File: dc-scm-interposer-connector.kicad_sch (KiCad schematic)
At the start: 19 parts, among them J2001 PinHeader_2x6_P2.54mm_Drill1.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

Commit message: [#103910] Update power section
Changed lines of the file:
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@@
-	(wire
-		(pts
-			(xy 142.24 85.09) (xy 142.24 86.36)
-		)
-		(stroke
-			(width 0)
-			(type default)
-		)
-	)
 	(wire
 		(pts
@@
 	(wire
 		(pts
-			(xy 142.24 88.9) (xy 144.78 88.9)
-		)
-		(stroke
-			(width 0)
-			(type default)
-		)
-	)
-	(wire
-		(pts
 			(xy 149.86 115.57) (xy 152.4 115.57)
 		)
@@
 	(wire
 		(pts
-			(xy 140.97 85.09) (xy 142.24 85.09)
+			(xy 127 86.36) (xy 144.78 86.36)
 		)
 		(stroke
@@
 		)
 	)
-	(wire
-		(pts
-			(xy 142.24 86.36) (xy 144.78 86.36)
-		)
-		(stroke
-			(width 0)
-			(type default)
-		)
-	)
 	(bus
 		(pts
@@
 	(wire
 		(pts
-			(xy 142.24 87.63) (xy 142.24 88.9)
-		)
-		(stroke
-			(width 0)
-			(type default)
-		)
-	)
-	(wire
-		(pts
-			(xy 149.86 119.38) (xy 152.4 119.38)
+			(xy 135.89 119.38) (xy 152.4 119.38)
 		)
 		(stroke
@@
 	(wire
 		(pts
-			(xy 140.97 87.63) (xy 142.24 87.63)
+			(xy 127 88.9) (xy 144.78 88.9)
 		)
 		(stroke
@@
 		)
 	)
+	(label "DC_SCM_12V_AUX"
+		(at 127 88.9 0)
+		(effects
+			(font
+				(size 1.27 1.27)
+			)
+			(justify left bottom)
+		)
+	)
 	(label "EC_ESPI.~{CS0}"
 		(at 149.86 128.27 180)
@@
 		)
 	)
+	(label "DC_SCM_12V_AUX"
+		(at 135.89 119.38 0)
+		(effects
+			(font
+				(size 1.27 1.27)
+			)
+			(justify left bottom)
+		)
+	)
 	(label "EC_ESPI.~{CS0}_R"
 		(at 123.19 93.98 0)
@@
 			)
 			(justify right bottom)
+		)
+	)
+	(label "DC_SCM_P3V0"
+		(at 127 86.36 0)
+		(effects
+			(font
+				(size 1.27 1.27)
+			)
+			(justify left bottom)
 		)
 	)
@@
 		)
 	)
-	(hierarchical_label "DC_SCM_P3V0"
-		(shape output)
-		(at 140.97 85.09 180)
-		(effects
-			(font
-				(size 1.27 1.27)
-			)
-			(justify right)
-		)
-	)
 	(hierarchical_label "DC_SCM_STBY_EN"
 		(shape output)
@@
 		(effects
 			(font
-				(size 1.27 1.27)
-			)
-			(justify right)
-		)
-	)
-	(hierarchical_label "DC_SCM_12V_AUX"
-		(shape output)
-		(at 149.86 119.38 180)
-		(effects
-			(font
-				(size 1.27 1.27)
-			)
-			(justify right)
-		)
-	)
-	(hierarchical_label "DC_SCM_12V_AUX"
-		(shape output)
-		(at 140.97 87.63 180)
-		(effects
-			(font

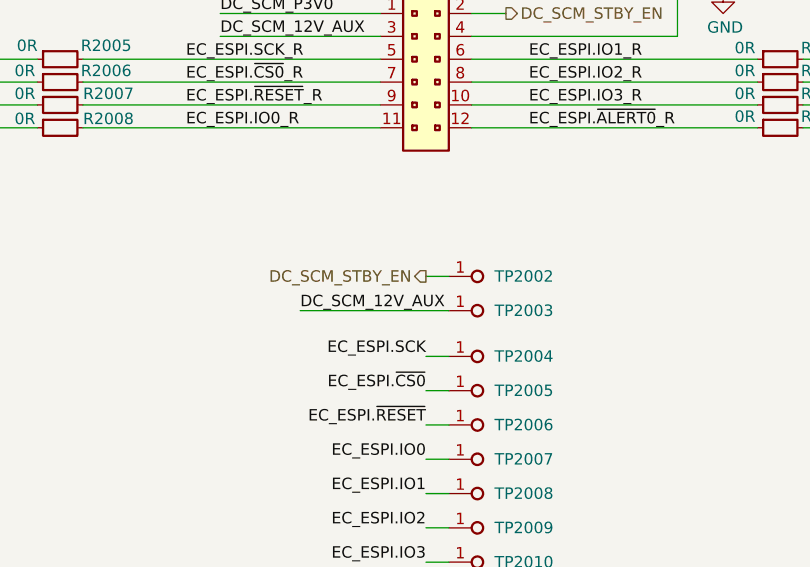
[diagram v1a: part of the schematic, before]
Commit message: [#103910] Annotate schematics & Clean ERC
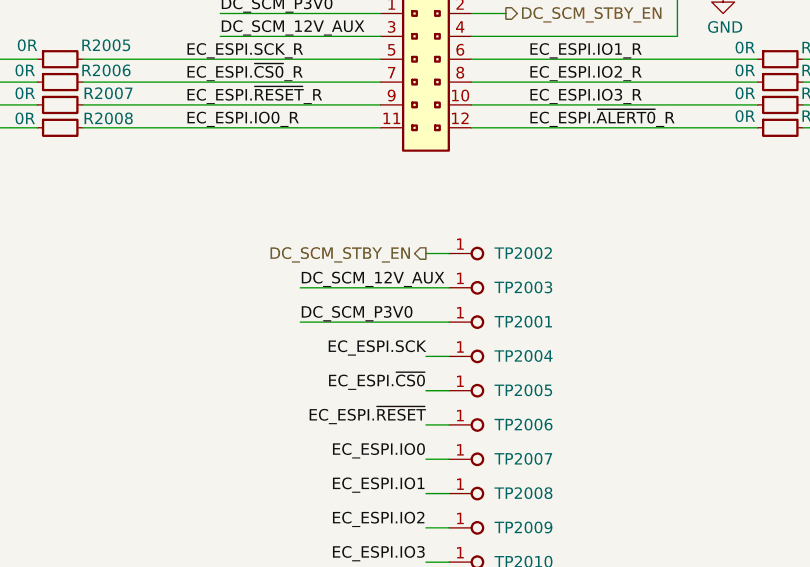
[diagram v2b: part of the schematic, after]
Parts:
- added TP2001: TP_1mm_SMD, antmicro-footprints:TP_SMD_1mm, symbol antmicroTestPoints:TP_1mm_SMD
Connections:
- net DC_SCM_P3V0: now also TP2001.1
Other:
- moved on the sheet: TP2002, TP2003
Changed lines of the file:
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@@
 	(wire
 		(pts
-			(xy 149.86 115.57) (xy 152.4 115.57)
+			(xy 149.86 113.03) (xy 152.4 113.03)
 		)
 		(stroke
@@
 	(wire
 		(pts
+			(xy 135.89 120.65) (xy 152.4 120.65)
+		)
+		(stroke
+			(width 0)
+			(type default)
+		)
+	)
+	(wire
+		(pts
 			(xy 149.86 124.46) (xy 152.4 124.46)
 		)
@@
 	(wire
 		(pts
-			(xy 135.89 119.38) (xy 152.4 119.38)
+			(xy 135.89 116.84) (xy 152.4 116.84)
 		)
 		(stroke
@@
 	)
 	(label "DC_SCM_12V_AUX"
-		(at 135.89 119.38 0)
+		(at 135.89 116.84 0)
 		(effects
 			(font
@@
 		)
 	)
+	(label "DC_SCM_P3V0"
+		(at 135.89 120.65 0)
+		(effects
+			(font
+				(size 1.27 1.27)
+			)
+			(justify left bottom)
+		)
+	)
 	(label "EC_ESPI.SCK"
 		(at 92.71 91.44 180)
@@
 	(hierarchical_label "DC_SCM_STBY_EN"
 		(shape output)
-		(at 149.86 115.57 180)
+		(at 149.86 113.03 180)
 		(effects
 			(font
@@
 	(symbol
 		(lib_id "antmicroTestPoints:TP_1mm_SMD")
+		(at 152.4 120.65 0)
+		(unit 1)
+		(body_style 1)
+		(exclude_from_sim no)
+		(in_bom no)
+		(on_board yes)
+		(in_pos_files yes)
+		(dnp no)
+		(fields_autoplaced yes)
+		(property "Reference" "TP2001"
+			(at 157.48 120.65 0)
+			(show_name no)
+			(do_not_autoplace no)
+			(effects
+				(font
+					(size 1.27 1.27)
+					(thickness 0.15)
+				)
+				(justify left)
+			)
+		)
+		(property "Value" "TP_1mm_SMD"
+			(at 167.64 128.27 0)
+			(hide yes)
+			(show_name no)
+			(do_not_autoplace no)
+			(effects
+				(font
+					(size 1.27 1.27)
+					(thickness 0.15)
+				)
+				(justify left bottom)
+			)
+		)
+		(property "Footprint" "antmicro-footprints:TP_SMD_1mm"
+			(at 167.64 130.81 0)
+			(hide yes)
+			(show_name no)
+			(do_not_autoplace no)
+			(effects
+				(font
+					(size 1.27 1.27)
+					(thickness 0.15)
+				)
+				(justify left bottom)
+			)
+		)
+		(property "Datasheet" ""
+			(at 170.18 133.35 0)
+			(hide yes)
+			(show_name no)
+			(do_not_autoplace no)
+			(effects
+				(font
+					(size 1.27 1.27)
+					(thickness 0.15)
+				)
+				(justify left bottom)
+			)
+		)
+		(property "Description" "Test point 1mm SMD"
+			(at 167.64 140.97 0)
+			(hide yes)
+			(show_name no)
+			(do_not_autoplace no)
+			(effects
+				(font
+					(size 1.27 1.27)
+				)
+				(justify left bottom)
+			)
+		)
+		(property "MPN" ""
+			(at 152.4 120.65 0)
+			(hide yes)
+			(show_name no)
+			(do_not_autoplace no)
+			(effects
+				(font
+					(size 1.27 1.27)
+				)
+			)
+		)
+		(property "Manufacturer" ""
+			(at 152.4 120.65 0)
+			(hide yes)
+			(show_name no)
+			(do_not_autoplace no)
+			(effects
+				(font
+					(size 1.27 1.27)
+				)
+			)
+		)
+		(property "Author" "Antmicro"
+			(at 167.64 135.89 0)
+			(hide yes)
+			(show_name no)
+			(do_not_autoplace no)
+			(effects
+				(font
+					(size 1.27 1.27)
+					(thickness 0.15)
+				)
+				(justify left bottom)
+			)
+		)
+		(property "License" "Apache-2.0"
+			(at 167.64 138.43 0)
+			(hide yes)
+			(show_name no)
+			(do_not_autoplace no)
+			(effects
+				(font
+					(size 1.27 1.27)
+					(thickness 0.15)
+				)
+				(justify left bottom)
+			)
+		)
+		(pin "1"
+		)
+		(instances
+			(project "machxo5-espi-debugger"
+				(path "/df391740-647e-4ab6-9dcd-d61184d66fe9/dad11b40-64da-40df-af81-feff62248020"
+					(reference "TP2001")
+					(unit 1)
+				)
+			)
+		)
+	)
+	(symbol
+		(lib_id "antmicroTestPoints:TP_1mm_SMD")
 		(at 152.4 124.46 0)
 		(unit 1)
@@
 	(symbol
 		(lib_id "antmicroTestPoints:TP_1mm_SMD")
-		(at 152.4 115.57 0)
+		(at 152.4 113.03 0)
 		(unit 1)
 		(body_style 1)
@@
 		(fields_autoplaced yes)
 		(property "Reference" "TP2002"
-			(at 157.48 115.57 0)
+			(at 157.48 113.03 0)
 			(show_name no)
 			(do_not_autoplace no)
@@
 		)
 		(property "Value" "TP_1mm_SMD"
-			(at 167.64 123.19 0)
+			(at 167.64 120.65 0)
 			(hide yes)
 			(show_name no)
@@
 		)
 		(property "Footprint" "antmicro-footprints:TP_SMD_1mm"
-			(at 167.64 125.73 0)
+			(at 167.64 123.19 0)
 			(hide yes)
 			(show_name no)
@@
 		)
 		(property "Datasheet" ""
-			(at 170.18 128.27 0)
+			(at 170.18 125.73 0)
 			(hide yes)
 			(show_name no)
@@
 		)
 		(property "Description" "Test point 1mm SMD"
-			(at 167.64 135.89 0)
+			(at 167.64 133.35 0)
 			(hide yes)
 			(show_name no)
@@
 		)
 		(property "MPN" ""
-			(at 152.4 115.57 0)
+			(at 152.4 113.03 0)
 			(hide yes)
 			(show_name no)
@@
 		)
 		(property "Manufacturer" ""
-			(at 152.4 115.57 0)
+			(at 152.4 113.03 0)
 			(hide yes)
 			(show_name no)
@@
 		)
 		(property "Author" "Antmicro"
-			(at 167.64 130.81 0)
+			(at 167.64 128.27 0)
 			(hide yes)
 			(show_name no)
@@
 		)
 		(property "License" "Apache-2.0"
-			(at 167.64 133.35 0)
+			(at 167.64 130.81 0)
 			(hide yes)
 			(show_name no)
@@
 	(symbol
 		(lib_id "antmicroTestPoints:TP_1mm_SMD")
-		(at 152.4 119.38 0)
+		(at 152.4 116.84 0)
 		(unit 1)
 		(body_style 1)
@@
 		(fields_autoplaced yes)
 		(property "Reference" "TP2003"
-			(at 157.48 119.38 0)
+			(at 157.48 116.84 0)
 			(show_name no)
 			(do_not_autoplace no)
@@
 		)
 		(property "Value" "TP_1mm_SMD"
-			(at 167.64 127 0)
+			(at 167.64 124.46 0)
 			(hide yes)
 			(show_name no)
@@
 		)
 		(property "Footprint" "antmicro-footprints:TP_SMD_1mm"
-			(at 167.64 129.54 0)
+			(at 167.64 127 0)
 			(hide yes)
 			(show_name no)
@@
 		)
 		(property "Datasheet" ""
-			(at 170.18 132.08 0)
+			(at 170.18 129.54 0)
 			(hide yes)
 			(show_name no)
@@
 		)
 		(property "Description" "Test point 1mm SMD"
-			(at 167.64 139.7 0)
+			(at 167.64 137.16 0)
 			(hide yes)
 			(show_name no)
@@
 		)
 		(property "MPN" ""
-			(at 152.4 119.38 0)
+			(at 152.4 116.84 0)
 			(hide yes)
 			(show_name no)
@@
 		)
 		(property "Manufacturer" ""
-			(at 152.4 119.38 0)
+			(at 152.4 116.84 0)
 			(hide yes)
 			(show_name no)
@@
 		)
 		(property "Author" "Antmicro"
-			(at 167.64 134.62 0)
+			(at 167.64 132.08 0)
 			(hide yes)
 			(show_name no)
@@
 		)
 		(property "License" "Apache-2.0"
-			(at 167.64 137.16 0)
+			(at 167.64 134.62 0)
 			(hide yes)
 			(show_name no)

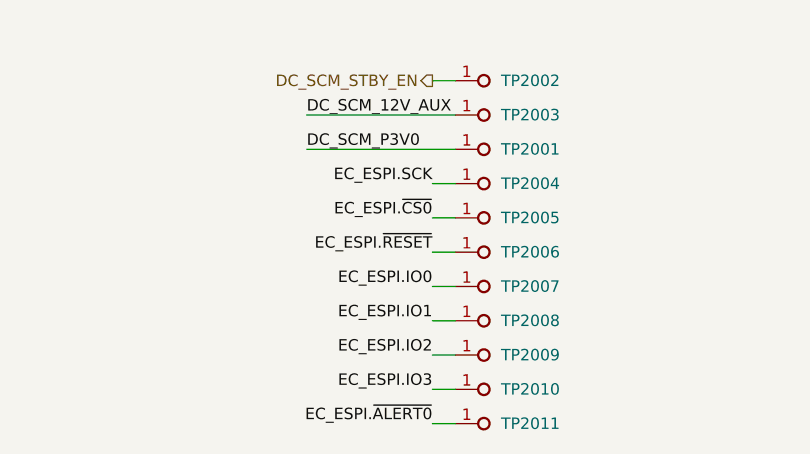
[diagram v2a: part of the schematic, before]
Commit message: [#103910] Sch: remove testpoints on SPI
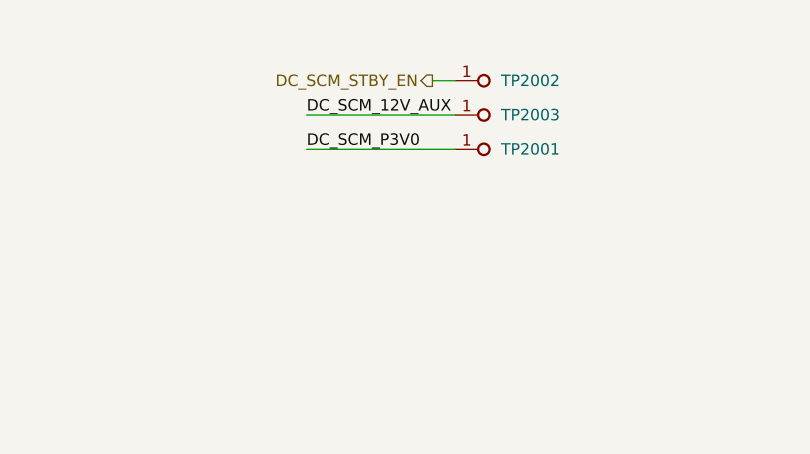
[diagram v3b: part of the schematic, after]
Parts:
- removed TP2004, TP2005, TP2006, TP2007, TP2008, TP2009, TP2010, TP2011: TP_1mm_SMD, antmicro-footprints:TP_SMD_1mm, symbol antmicroTestPoints:TP_1mm_SMD

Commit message: [#103953] sch/pcb: re-annotate components
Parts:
- renumbered J2001 to J1, R2005 to R1, R2006 to R2, R2007 to R3, R2008 to R4, R2001 to R5, R2002 to R6, R2003 to R7, R2004 to R8, TP2002 to TP1, TP2003 to TP2, TP2001 to TP3
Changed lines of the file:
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@@
 		(in_pos_files yes)
 		(dnp no)
-		(property "Reference" "J2001"
+		(property "Reference" "J1"
 			(at 146.558 79.502 0)
 			(show_name no)
@@
 			(project "machxo5-espi-debugger"
 				(path "/df391740-647e-4ab6-9dcd-d61184d66fe9/dad11b40-64da-40df-af81-feff62248020"
-					(reference "J2001")
+					(reference "J1")
 					(unit 1)
 				)
@@
 		(in_pos_files yes)
 		(dnp no)
-		(property "Reference" "R2007"
+		(property "Reference" "R3"
 			(at 111.76 96.012 0)
 			(show_name no)
@@
 			(project "machxo5-espi-debugger"
 				(path "/df391740-647e-4ab6-9dcd-d61184d66fe9/dad11b40-64da-40df-af81-feff62248020"
-					(reference "R2007")
+					(reference "R3")
 					(unit 1)
 				)
@@
 		(in_pos_files yes)
 		(dnp no)
-		(property "Reference" "R2003"
+		(property "Reference" "R7"
 			(at 191.516 96.012 0)
 			(show_name no)
@@
 			(project "machxo5-espi-debugger"
 				(path "/df391740-647e-4ab6-9dcd-d61184d66fe9/dad11b40-64da-40df-af81-feff62248020"
-					(reference "R2003")
+					(reference "R7")
 					(unit 1)
 				)
@@
 		(in_pos_files yes)
 		(dnp no)
-		(property "Reference" "R2004"
+		(property "Reference" "R8"
 			(at 191.516 98.552 0)
 			(show_name no)
@@
 			(project "machxo5-espi-debugger"
 				(path "/df391740-647e-4ab6-9dcd-d61184d66fe9/dad11b40-64da-40df-af81-feff62248020"
-					(reference "R2004")
+					(reference "R8")
 					(unit 1)
 				)
@@
 		(in_pos_files yes)
 		(dnp no)
-		(property "Reference" "#PWR2001"
+		(property "Reference" "#PWR02"
 			(at 191.77 86.36 0)
 			(hide yes)
@@
 			(project "machxo5-espi-debugger"
 				(path "/df391740-647e-4ab6-9dcd-d61184d66fe9/dad11b40-64da-40df-af81-feff62248020"
-					(reference "#PWR2001")
+					(reference "#PWR02")
 					(unit 1)
 				)
@@
 		(in_pos_files yes)
 		(dnp no)
-		(property "Reference" "R2001"
+		(property "Reference" "R5"
 			(at 191.516 90.932 0)
 			(show_name no)
@@
 			(project "machxo5-espi-debugger"
 				(path "/df391740-647e-4ab6-9dcd-d61184d66fe9/dad11b40-64da-40df-af81-feff62248020"
-					(reference "R2001")
+					(reference "R5")
 					(unit 1)
 				)
@@
 		(dnp no)
 		(fields_autoplaced yes)
-		(property "Reference" "TP2001"
+		(property "Reference" "TP3"
 			(at 157.48 120.65 0)
 			(show_name no)
@@
 			(project "machxo5-espi-debugger"
 				(path "/df391740-647e-4ab6-9dcd-d61184d66fe9/dad11b40-64da-40df-af81-feff62248020"
-					(reference "TP2001")
+					(reference "TP3")
 					(unit 1)
 				)
@@
 		(dnp no)
 		(fields_autoplaced yes)
-		(property "Reference" "TP2002"
+		(property "Reference" "TP1"
 			(at 157.48 113.03 0)
 			(show_name no)
@@
 			(project "machxo5-espi-debugger"
 				(path "/df391740-647e-4ab6-9dcd-d61184d66fe9/dad11b40-64da-40df-af81-feff62248020"
-					(reference "TP2002")
+					(reference "TP1")
 					(unit 1)
 				)
@@
 		(in_pos_files yes)
 		(dnp no)
-		(property "Reference" "R2006"
+		(property "Reference" "R2"
 			(at 111.506 93.472 0)
 			(show_name no)
@@
 			(project "machxo5-espi-debugger"
 				(path "/df391740-647e-4ab6-9dcd-d61184d66fe9/dad11b40-64da-40df-af81-feff62248020"
-					(reference "R2006")
+					(reference "R2")
 					(unit 1)
 				)
@@
 		(dnp no)
 		(fields_autoplaced yes)
-		(property "Reference" "TP2003"
+		(property "Reference" "TP2"
 			(at 157.48 116.84 0)
 			(show_name no)
@@
 			(project "machxo5-espi-debugger"
 				(path "/df391740-647e-4ab6-9dcd-d61184d66fe9/dad11b40-64da-40df-af81-feff62248020"
-					(reference "TP2003")
+					(reference "TP2")
 					(unit 1)
 				)
@@
 		(in_pos_files yes)
 		(dnp no)
-		(property "Reference" "R2005"
+		(property "Reference" "R1"
 			(at 111.506 90.678 0)
 			(show_name no)
@@
 			(project "machxo5-espi-debugger"
 				(path "/df391740-647e-4ab6-9dcd-d61184d66fe9/dad11b40-64da-40df-af81-feff62248020"
-					(reference "R2005")
+					(reference "R1")
 					(unit 1)
 				)
@@
 		(in_pos_files yes)
 		(dnp no)
-		(property "Reference" "R2008"
+		(property "Reference" "R4"
 			(at 111.76 98.806 0)
 			(show_name no)
@@
 			(project "machxo5-espi-debugger"
 				(path "/df391740-647e-4ab6-9dcd-d61184d66fe9/dad11b40-64da-40df-af81-feff62248020"
-					(reference "R2008")
+					(reference "R4")
 					(unit 1)
 				)
@@
 		(in_pos_files yes)
 		(dnp no)
-		(property "Reference" "R2002"
+		(property "Reference" "R6"
 			(at 191.516 93.472 0)
 			(show_name no)
@@
 			(project "machxo5-espi-debugger"
 				(path "/df391740-647e-4ab6-9dcd-d61184d66fe9/dad11b40-64da-40df-af81-feff62248020"
-					(reference "R2002")
+					(reference "R6")
 					(unit 1)
 				)
